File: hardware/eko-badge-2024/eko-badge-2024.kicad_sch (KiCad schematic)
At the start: 53 parts, among them J1 UART, J2 Battery, J3 Lentes, J4 OLED, J5 Add-On, J6 Add-On, J7 Battery, P1 USB_C_Plug_USB2.0, Q1 DMG3415U-7, SW1 ON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

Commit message: feat(Hw):Added_Speaker_Holes
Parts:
- AE1: footprint Eko2024:SMA_EDGE -> Connector_PinHeader_2.54mm:PinHeader_1x01_P2.54mm_Vertical
- J3: footprint Connector_PinSocket_2.54mm:PinSocket_2x03_P2.54mm_Vertical -> Connector_PinSocket_2.54mm:PinSocket_2x03_P2.54mm_Vertical_SMD; LCSC# C124421 -> (none); Proveedor Digikey -> DIGIKEY; manf# PPPC032LFBN-RC -> HLE-103-02-L-DV
- LS1: footprint Connector_PinHeader_1.27mm:PinHeader_1x02_P1.27mm_Vertical -> Connector_PinHeader_2.54mm:PinHeader_1x02_P2.54mm_Vertical
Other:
- company: (none) -> ElectronicCats
- title: (none) -> Ekoparty 2024
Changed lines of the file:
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@@
 	(generator_version "8.0")
 	(paper "A4")
+	(title_block
+		(title "Ekoparty 2024")
+		(date "2024-08-28")
+		(rev "1.0")
+		(company "ElectronicCats")
+		(comment 1 "Edgar Capuchino")
+	)
 	(junction
 		(at 140.208 92.71)
@@
 			)
 		)
-		(property "Footprint" "Connector_PinHeader_1.27mm:PinHeader_1x02_P1.27mm_Vertical"
+		(property "Footprint" "Connector_PinHeader_2.54mm:PinHeader_1x02_P2.54mm_Vertical"
 			(at 252.476 93.472 0)
 			(effects
@@
 			)
 		)
-		(property "Footprint" "Eko2024:SMA_EDGE"
+		(property "Footprint" "Connector_PinHeader_2.54mm:PinHeader_1x01_P2.54mm_Vertical"
 			(at 259.588 121.158 0)
 			(effects
@@
 			)
 		)
-		(property "Footprint" "Connector_PinSocket_2.54mm:PinSocket_2x03_P2.54mm_Vertical"
+		(property "Footprint" "Connector_PinSocket_2.54mm:PinSocket_2x03_P2.54mm_Vertical_SMD"
 			(at 72.39 184.15 0)
 			(effects
@@
 			)
 		)
-		(property "LCSC#" "C124421"
+		(property "LCSC#" ""
 			(at 72.39 184.15 0)
 			(effects
@@
 			)
 		)
-		(property "Proveedor" "Digikey"
+		(property "Proveedor" "DIGIKEY"
 			(at 72.39 184.15 0)
 			(effects
@@
 			)
 		)
-		(property "manf#" "PPPC032LFBN-RC"
+		(property "manf#" "HLE-103-02-L-DV"
 			(at 72.39 184.15 0)
 			(effects

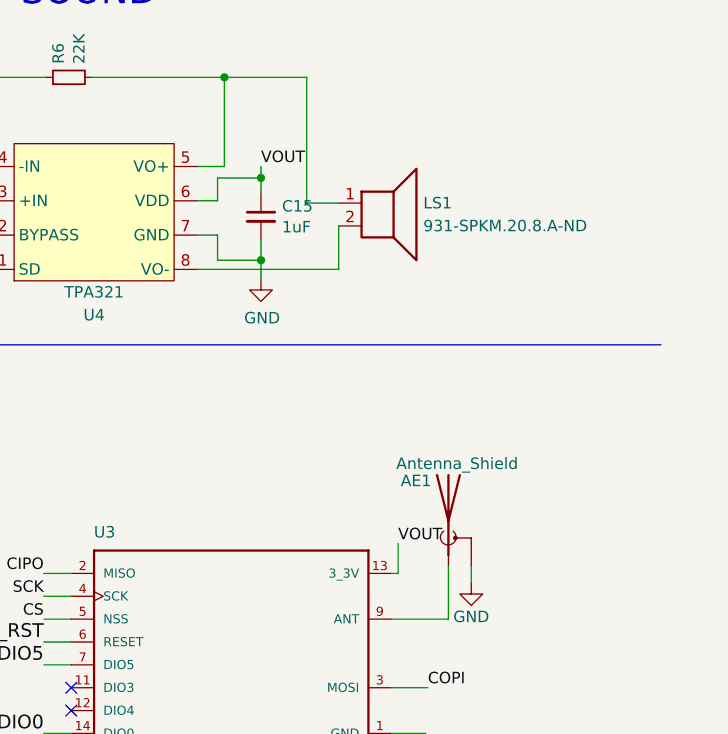
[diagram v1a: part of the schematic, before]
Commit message: feat(Hw):Update_Connector_Pinsocket
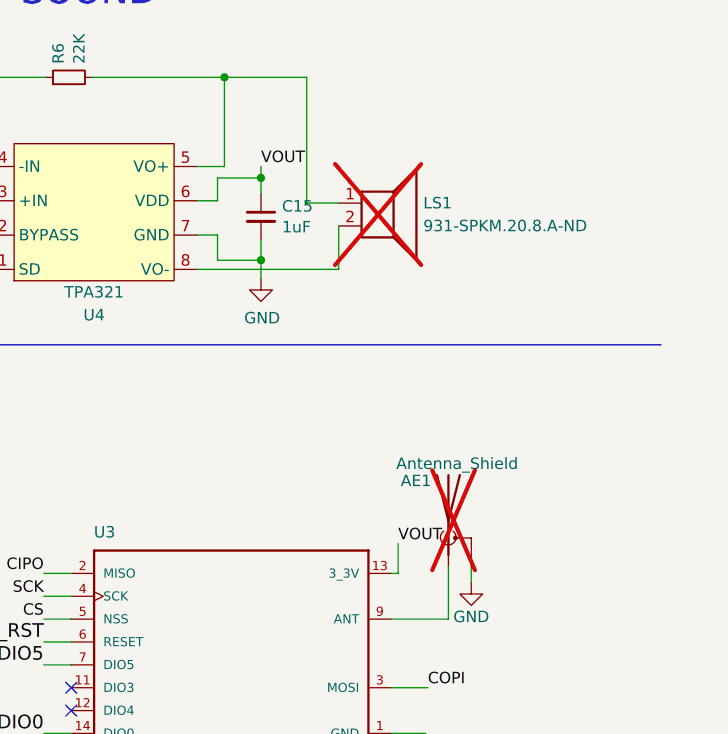
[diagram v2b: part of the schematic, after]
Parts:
- AE1, LS1: now not fitted
- J3: footprint Connector_PinSocket_2.54mm:PinSocket_2x03_P2.54mm_Vertical_SMD -> Eko2024:HARWIN_M20-7810345; manf# HLE-103-02-L-DV -> M20-7810345
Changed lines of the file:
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@@
 		(in_bom yes)
 		(on_board yes)
-		(dnp no)
+		(dnp yes)
 		(fields_autoplaced yes)
 		(property "Reference" "LS1"
@@
 		(in_bom yes)
 		(on_board yes)
-		(dnp no)
+		(dnp yes)
 		(property "Reference" "AE1"
 			(at 257.683 119.253 0)
@@
 			)
 		)
-		(property "Footprint" "Connector_PinSocket_2.54mm:PinSocket_2x03_P2.54mm_Vertical_SMD"
+		(property "Footprint" "Eko2024:HARWIN_M20-7810345"
 			(at 72.39 184.15 0)
 			(effects
@@
 			)
 		)
-		(property "manf#" "HLE-103-02-L-DV"
+		(property "manf#" "M20-7810345 "
 			(at 72.39 184.15 0)
 			(effects

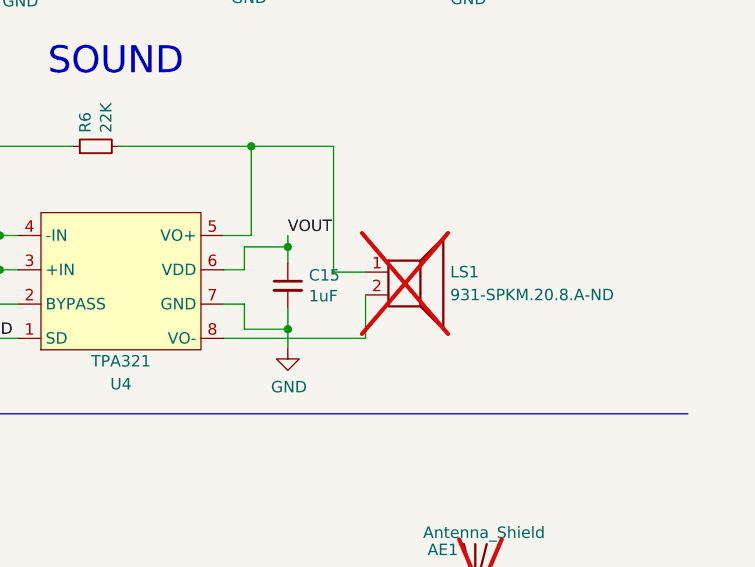
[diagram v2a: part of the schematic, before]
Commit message: feat(Hw):Update_BoM
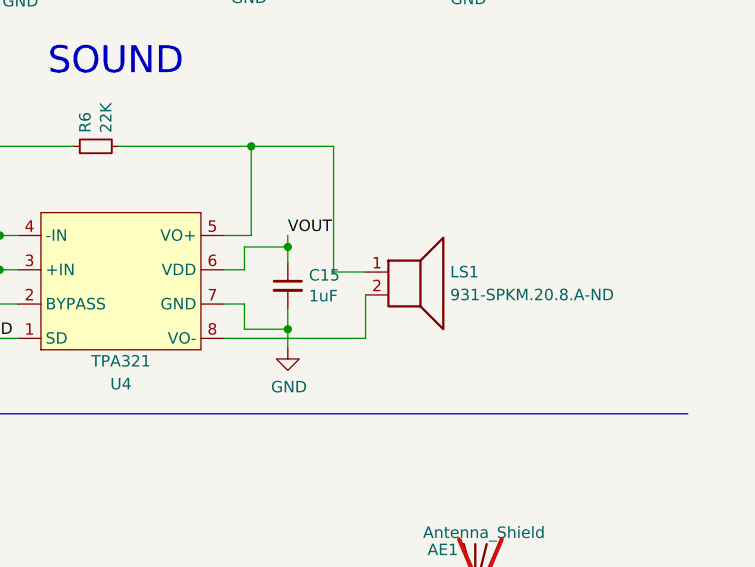
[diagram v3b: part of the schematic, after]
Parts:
- LS1: now fitted
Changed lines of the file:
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@@
 		(in_bom yes)
 		(on_board yes)
-		(dnp yes)
+		(dnp no)
 		(fields_autoplaced yes)
 		(property "Reference" "LS1"
